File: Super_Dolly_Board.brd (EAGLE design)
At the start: 154.5 x 44.5 mm, 89 parts, among them IC1 AT90USB646-AU, J1 10118193-0001LF, J3 SJ1-2503A, J4 RJHS-538X, J5 SJ1-2503A, P1 TC33X-2, SW1 SKQUDBE010, U1 AT90USB646-MU, U2 MMDT3904, U3 TB6559FG, U4 TS2937CW50, U5 TB6559FG, U6 SN75176BDR, U7 TB6559FG, U8 TPD2E007DCK, U9 TS2937CW50, X1 3.2X2.5MMCRYSTAL

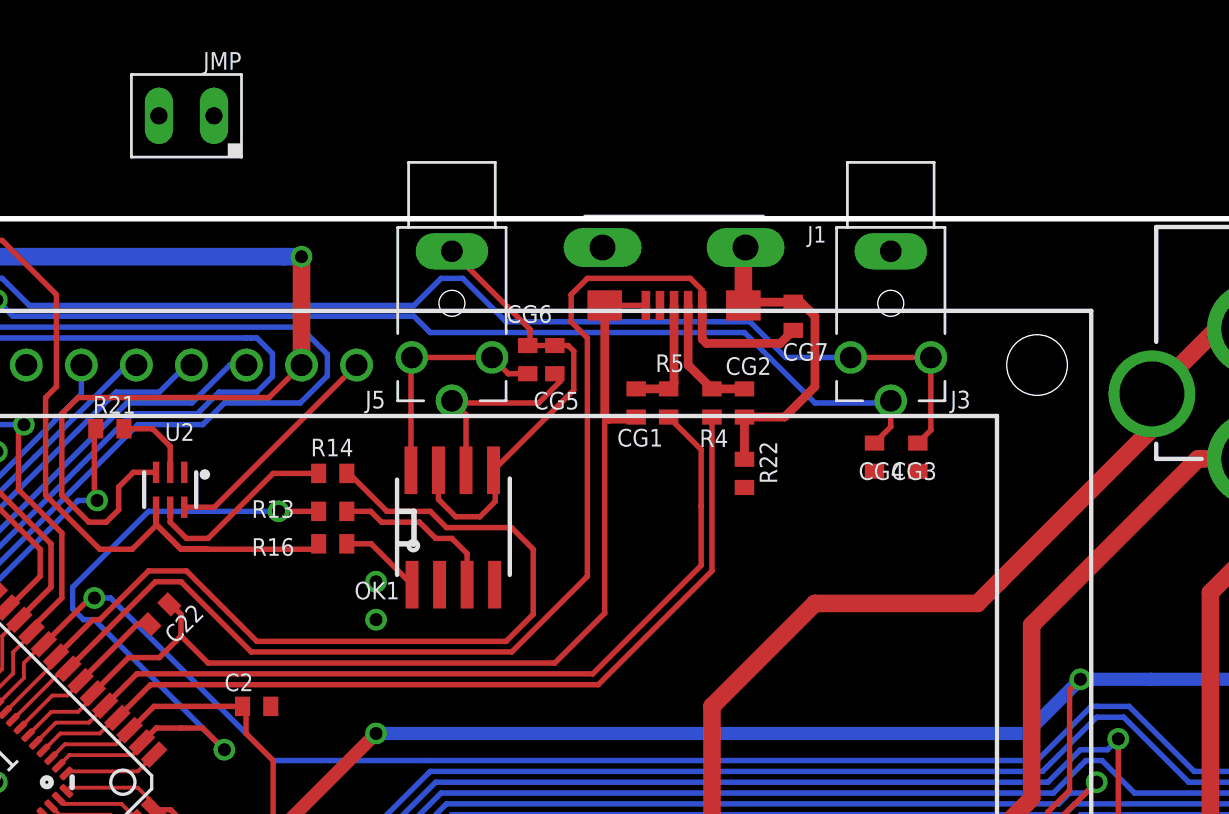
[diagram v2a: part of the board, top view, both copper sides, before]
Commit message: added jumper to bridge VUSB and +5V so the usb can power the device for testing
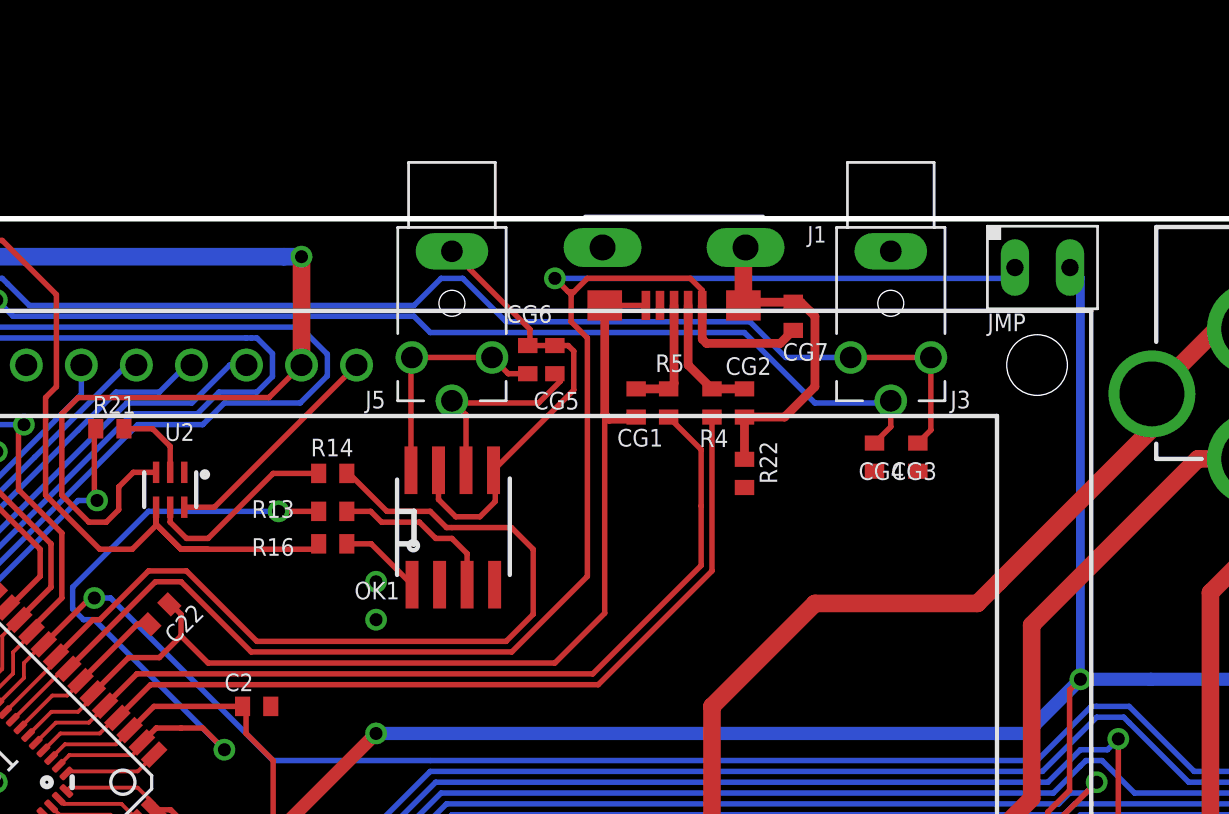
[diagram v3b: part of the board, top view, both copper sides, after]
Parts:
- moved JMP 40.1 mm to (37.8, 16.8), turned to 0 degrees
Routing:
- net VUSB: track 60.2 -> 82.7 mm, vias 0 -> 1
- net +5V: track 473.1 -> 492.3 mm
- net GND: vias 47 -> 111
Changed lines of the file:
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@@
 <element name="R26" library="parkers_parts" package="0402_RES" value="20K" x="7.5" y="-16.25" rot="R180"/>
 <element name="U1" library="at90usb" package="MLF64" value="AT90USB646-MU" x="-13" y="-7" rot="R225"/>
-<element name="JMP" library="parkers_parts" package="P1X02" value="P1X02PH" x="-1.75" y="23.75" rot="R180"/>
+<element name="JMP" library="parkers_parts" package="P1X02" value="P1X02PH" x="37.75" y="16.75"/>
 </elements>
 <signals>
@@
 <via x="77.75" y="-7.5" extent="1-16" drill="0.6"/>
 <wire x1="77.75" y1="-7.5" x2="77.25" y2="-7.5" width="0.254" layer="16"/>
+<wire x1="39.02" y1="16.75" x2="39.5" y2="16.27" width="0.4064" layer="16"/>
+<wire x1="39.5" y1="16.27" x2="39.5" y2="-2.25" width="0.4064" layer="16"/>
 <wire x1="-6" y1="-17.5" x2="-7.45961875" y2="-17.631546875" width="0" layer="19" extent="1-16"/>
-<wire x1="-3.02" y1="23.75" x2="2.75" y2="17.25" width="0" layer="19" extent="16-16"/>
 </signal>
 <signal name="GND">
@@
 <via x="50.25" y="-21.75" extent="1-16" drill="0.6"/>
 <via x="48.75" y="-21.75" extent="1-16" drill="0.6"/>
+<via x="24.5" y="-11" extent="1-16" drill="0.6"/>
+<via x="28.5" y="-11" extent="1-16" drill="0.6"/>
+<via x="27.25" y="-11" extent="1-16" drill="0.6"/>
+<via x="25.75" y="-11" extent="1-16" drill="0.6"/>
+<via x="24.5" y="-12.5" extent="1-16" drill="0.6"/>
+<via x="28.5" y="-12.5" extent="1-16" drill="0.6"/>
+<via x="27.25" y="-12.5" extent="1-16" drill="0.6"/>
+<via x="25.75" y="-12.5" extent="1-16" drill="0.6"/>
+<via x="24.5" y="-14" extent="1-16" drill="0.6"/>
+<via x="28.5" y="-14" extent="1-16" drill="0.6"/>
+<via x="27.25" y="-14" extent="1-16" drill="0.6"/>
+<via x="25.75" y="-14" extent="1-16" drill="0.6"/>
+<via x="24.5" y="-15.5" extent="1-16" drill="0.6"/>
+<via x="28.5" y="-15.5" extent="1-16" drill="0.6"/>
+<via x="27.25" y="-15.5" extent="1-16" drill="0.6"/>
+<via x="25.75" y="-15.5" extent="1-16" drill="0.6"/>
+<via x="24.5" y="-17.25" extent="1-16" drill="0.6"/>
+<via x="28.5" y="-17.25" extent="1-16" drill="0.6"/>
+<via x="27.25" y="-17.25" extent="1-16" drill="0.6"/>
+<via x="25.75" y="-17.25" extent="1-16" drill="0.6"/>
+<via x="24.5" y="-18.75" extent="1-16" drill="0.6"/>
+<via x="28.5" y="-18.75" extent="1-16" drill="0.6"/>
+<via x="27.25" y="-18.75" extent="1-16" drill="0.6"/>
+<via x="25.75" y="-18.75" extent="1-16" drill="0.6"/>
+<via x="24.5" y="-20.25" extent="1-16" drill="0.6"/>
+<via x="28.5" y="-20.25" extent="1-16" drill="0.6"/>
+<via x="27.25" y="-20.25" extent="1-16" drill="0.6"/>
+<via x="25.75" y="-20.25" extent="1-16" drill="0.6"/>
+<via x="24.5" y="-21.75" extent="1-16" drill="0.6"/>
+<via x="28.5" y="-21.75" extent="1-16" drill="0.6"/>
+<via x="27.25" y="-21.75" extent="1-16" drill="0.6"/>
+<via x="25.75" y="-21.75" extent="1-16" drill="0.6"/>
+<via x="67" y="-11.5" extent="1-16" drill="0.6"/>
+<via x="71" y="-11.5" extent="1-16" drill="0.6"/>
+<via x="69.75" y="-11.5" extent="1-16" drill="0.6"/>
+<via x="68.25" y="-11.5" extent="1-16" drill="0.6"/>
+<via x="67" y="-13" extent="1-16" drill="0.6"/>
+<via x="71" y="-13" extent="1-16" drill="0.6"/>
+<via x="69.75" y="-13" extent="1-16" drill="0.6"/>
+<via x="68.25" y="-13" extent="1-16" drill="0.6"/>
+<via x="67" y="-14.5" extent="1-16" drill="0.6"/>
+<via x="71" y="-14.5" extent="1-16" drill="0.6"/>
+<via x="69.75" y="-14.5" extent="1-16" drill="0.6"/>
+<via x="68.25" y="-14.5" extent="1-16" drill="0.6"/>
+<via x="67" y="-16" extent="1-16" drill="0.6"/>
+<via x="71" y="-16" extent="1-16" drill="0.6"/>
+<via x="69.75" y="-16" extent="1-16" drill="0.6"/>
+<via x="68.25" y="-16" extent="1-16" drill="0.6"/>
+<via x="67" y="-17.25" extent="1-16" drill="0.6"/>
+<via x="71" y="-17.25" extent="1-16" drill="0.6"/>
+<via x="69.75" y="-17.25" extent="1-16" drill="0.6"/>
+<via x="68.25" y="-17.25" extent="1-16" drill="0.6"/>
+<via x="67" y="-18.75" extent="1-16" drill="0.6"/>
+<via x="71" y="-18.75" extent="1-16" drill="0.6"/>
+<via x="69.75" y="-18.75" extent="1-16" drill="0.6"/>
+<via x="68.25" y="-18.75" extent="1-16" drill="0.6"/>
+<via x="67" y="-20.25" extent="1-16" drill="0.6"/>
+<via x="71" y="-20.25" extent="1-16" drill="0.6"/>
+<via x="69.75" y="-20.25" extent="1-16" drill="0.6"/>
+<via x="68.25" y="-20.25" extent="1-16" drill="0.6"/>
+<via x="67" y="-21.75" extent="1-16" drill="0.6"/>
+<via x="71" y="-21.75" extent="1-16" drill="0.6"/>
+<via x="69.75" y="-21.75" extent="1-16" drill="0.6"/>
+<via x="68.25" y="-21.75" extent="1-16" drill="0.6"/>
 </signal>
 <signal name="AREF" class="4">
@@
 <wire x1="22.05" y1="15.7" x2="21.5" y2="16.25" width="0.254" layer="1"/>
 <wire x1="21.5" y1="16.25" x2="16.75" y2="16.25" width="0.254" layer="1"/>
-<wire x1="16.75" y1="16.25" x2="16" y2="15.5" width="0.254" layer="1"/>
+<wire x1="16.75" y1="16.25" x2="16.125" y2="15.625" width="0.254" layer="1"/>
+<wire x1="16.125" y1="15.625" x2="16" y2="15.5" width="0.254" layer="1"/>
 <wire x1="16" y1="15.5" x2="16" y2="14.25" width="0.254" layer="1"/>
 <wire x1="16" y1="14.25" x2="16.75" y2="13.5" width="0.254" layer="1"/>
@@
 <wire x1="-2" y1="2.25" x2="-3.1843125" y2="2.25" width="0.254" layer="1"/>
 <wire x1="-3.1843125" y1="2.25" x2="-7.201721875" y2="-1.767409375" width="0.254" layer="1"/>
-<wire x1="16" y1="15.5" x2="-0.48" y2="23.75" width="0" layer="19" extent="1-1"/>
+<wire x1="36.48" y1="16.75" x2="35.98" y2="16.25" width="0.254" layer="16"/>
+<wire x1="35.98" y1="16.25" x2="15.25" y2="16.25" width="0.254" layer="16"/>
+<via x="15.25" y="16.25" extent="1-16" drill="0.6"/>
+<wire x1="15.25" y1="16.25" x2="15.875" y2="15.625" width="0.254" layer="1"/>
+<wire x1="15.875" y1="15.625" x2="16.125" y2="15.625" width="0.254" layer="1"/>
 </signal>
 <signal name="UCAP">
@@
 <wire x1="-18.596190625" y1="-6" x2="-18.35633125" y2="-6.239859375" width="0" layer="19" extent="1-1"/>
 </signal>
-<signal name="GND1">
-<via x="67" y="-11.5" extent="1-16" drill="0.6"/>
-<via x="71" y="-11.5" extent="1-16" drill="0.6"/>
-<via x="69.75" y="-11.5" extent="1-16" drill="0.6"/>
-<via x="68.25" y="-11.5" extent="1-16" drill="0.6"/>
-<via x="67" y="-13" extent="1-16" drill="0.6"/>
-<via x="71" y="-13" extent="1-16" drill="0.6"/>
-<via x="69.75" y="-13" extent="1-16" drill="0.6"/>
-<via x="68.25" y="-13" extent="1-16" drill="0.6"/>
-<via x="67" y="-14.5" extent="1-16" drill="0.6"/>
-<via x="71" y="-14.5" extent="1-16" drill="0.6"/>
-<via x="69.75" y="-14.5" extent="1-16" drill="0.6"/>
-<via x="68.25" y="-14.5" extent="1-16" drill="0.6"/>
-<via x="67" y="-16" extent="1-16" drill="0.6"/>
-<via x="71" y="-16" extent="1-16" drill="0.6"/>
-<via x="69.75" y="-16" extent="1-16" drill="0.6"/>
-<via x="68.25" y="-16" extent="1-16" drill="0.6"/>
-</signal>
-<signal name="GND2">
-<via x="67" y="-17.25" extent="1-16" drill="0.6"/>
-<via x="71" y="-17.25" extent="1-16" drill="0.6"/>
-<via x="69.75" y="-17.25" extent="1-16" drill="0.6"/>
-<via x="68.25" y="-17.25" extent="1-16" drill="0.6"/>
-<via x="67" y="-18.75" extent="1-16" drill="0.6"/>
-<via x="71" y="-18.75" extent="1-16" drill="0.6"/>
-<via x="69.75" y="-18.75" extent="1-16" drill="0.6"/>
-<via x="68.25" y="-18.75" extent="1-16" drill="0.6"/>
-<via x="67" y="-20.25" extent="1-16" drill="0.6"/>
-<via x="71" y="-20.25" extent="1-16" drill="0.6"/>
-<via x="69.75" y="-20.25" extent="1-16" drill="0.6"/>
-<via x="68.25" y="-20.25" extent="1-16" drill="0.6"/>
-<via x="67" y="-21.75" extent="1-16" drill="0.6"/>
-<via x="71" y="-21.75" extent="1-16" drill="0.6"/>
-<via x="69.75" y="-21.75" extent="1-16" drill="0.6"/>
-<via x="68.25" y="-21.75" extent="1-16" drill="0.6"/>
-</signal>
-<signal name="GND3">
-<via x="24.5" y="-11" extent="1-16" drill="0.6"/>
-<via x="28.5" y="-11" extent="1-16" drill="0.6"/>
-<via x="27.25" y="-11" extent="1-16" drill="0.6"/>
-<via x="25.75" y="-11" extent="1-16" drill="0.6"/>
-<via x="24.5" y="-12.5" extent="1-16" drill="0.6"/>
-<via x="28.5" y="-12.5" extent="1-16" drill="0.6"/>
-<via x="27.25" y="-12.5" extent="1-16" drill="0.6"/>
-<via x="25.75" y="-12.5" extent="1-16" drill="0.6"/>
-<via x="24.5" y="-14" extent="1-16" drill="0.6"/>
-<via x="28.5" y="-14" extent="1-16" drill="0.6"/>
-<via x="27.25" y="-14" extent="1-16" drill="0.6"/>
-<via x="25.75" y="-14" extent="1-16" drill="0.6"/>
-<via x="24.5" y="-15.5" extent="1-16" drill="0.6"/>
-<via x="28.5" y="-15.5" extent="1-16" drill="0.6"/>
-<via x="27.25" y="-15.5" extent="1-16" drill="0.6"/>
-<via x="25.75" y="-15.5" extent="1-16" drill="0.6"/>
-</signal>
-<signal name="GND4">
-<via x="24.5" y="-17.25" extent="1-16" drill="0.6"/>
-<via x="28.5" y="-17.25" extent="1-16" drill="0.6"/>
-<via x="27.25" y="-17.25" extent="1-16" drill="0.6"/>
-<via x="25.75" y="-17.25" extent="1-16" drill="0.6"/>
-<via x="24.5" y="-18.75" extent="1-16" drill="0.6"/>
-<via x="28.5" y="-18.75" extent="1-16" drill="0.6"/>
-<via x="27.25" y="-18.75" extent="1-16" drill="0.6"/>
-<via x="25.75" y="-18.75" extent="1-16" drill="0.6"/>
-<via x="24.5" y="-20.25" extent="1-16" drill="0.6"/>
-<via x="28.5" y="-20.25" extent="1-16" drill="0.6"/>
-<via x="27.25" y="-20.25" extent="1-16" drill="0.6"/>
-<via x="25.75" y="-20.25" extent="1-16" drill="0.6"/>
-<via x="24.5" y="-21.75" extent="1-16" drill="0.6"/>
-<via x="28.5" y="-21.75" extent="1-16" drill="0.6"/>
-<via x="27.25" y="-21.75" extent="1-16" drill="0.6"/>
-<via x="25.75" y="-21.75" extent="1-16" drill="0.6"/>
-</signal>
 </signals>
-<errors>
-</errors>
 </board>
 </drawing>

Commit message: finished SDB REV2
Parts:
- removed R25: 36K, parkers_parts:0402_RES
- removed R26: 20K, parkers_parts:0402_RES
- added C14: .1uF, parkers_parts:0402_CAP
- added D2: PMEG6010EP, parkers_parts:SOD-128
- added U10: IP4234CZ6, parkers_parts:SOT-457
- C10, C11, C8: value .1uF -> .1uF 35V
- D1: value PMEG3030EP -> PMEG6010EP
- J4: value RJHS-538X -> RJHSE-5381
- MOT0, MOT1, MOT2: value (none) -> KLDX-0202-B-LT
- PWR: value (none) -> KLDX-0202-A-LT
- R4: value 22 -> 4K
- R5: value 22 -> 20K
- moved CG4 69.0 mm to (-34.8, -9.50), turned to 270 degrees
- moved CG7 64.0 mm to (-37.0, 4.50), turned to 180 degrees
- moved CG1 60.1 mm to (-40.8, 4.50), turned to 180 degrees
- moved R5 31.6 mm to (7.50, -18.2), turned to 0 degrees
- moved R4 30.7 mm to (7.50, -16.2), turned to 180 degrees
- moved CG2 6.50 mm to (30.0, 8.00)
- moved R22 4.37 mm to (25.0, 11.5)
- moved CG3 2.00 mm to (32.0, 8.00)
- renumbered IC1 to U11
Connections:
- net 12VB: now also D2.CATHODE
- net BATT_V: now also C14.1, R4.2, R5.1; no longer R25.1, R26.2
- net COM1: now also CG4.1
- net COM2: now also CG7.1
- net COM3: now also CG1.2
- net D+: now also U10.1; no longer CG1.2, R5.1
- net D-: now also U10.6; no longer CG2.2, R4.1
- net GND: now also C14.2, CG1.1, CG2.1, CG4.2, CG7.2, D2.ANODE, R4.1; no longer CG4.1, R26.1
- net IO_2: now also CG2.2; no longer CG3.2
- net IO_3: now also CG3.2; no longer CG4.2
- net RD+: now also U10.3; no longer R5.2
- net RD-: now also U10.4; no longer R4.2
- net UGND: now also U10.2; no longer CG1.1, CG2.1, CG7.1
- net VIN: now also R5.2; no longer R25.2
- net VUSB: now also U10.5; no longer CG7.2
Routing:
- net GND: track 17.6 -> 48.6 mm, vias 111 -> 177
- net M2_P: track 114.2 -> 103.2 mm
- net UGND: track 67.8 -> 59.4 mm
- net COM2: track 46.2 -> 52.8 mm, vias 0 -> 2
- net 12VB: track 29.9 -> 33.0 mm
- net OK_SHT: track 55.4 -> 53.2 mm
- net COM3: track 45.7 -> 47.5 mm
- net BATT_V: track 20.7 -> 22.4 mm
- net RD-: track 41.4 -> 39.7 mm
- net M1_A: track 110.3 -> 111.9 mm
- net RD+: track 41.6 -> 40.1 mm
- net COM1: track 51.5 -> 52.8 mm
- net M2_B: track 101.2 -> 102.0 mm
- net M1_B: track 94.3 -> 95.0 mm
- net +5V: track 492.3 -> 493.0 mm
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
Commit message: finished REV2 of SDB
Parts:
- added AUX: (no value), pinhead:2X04
- added CG8, CG9: CG0402MLC-05LG, parkers_parts:0402_RES
- added J6: SJ1-2503A, parkers_parts:SJ1-2503A
- LCD1: value LCD-16X2 -> LCD-16X2NOHOLES; device SparkFun:LCD-16X2 -> SparkFun-Displays:LCD-16X2_NOHOLES
- moved CG6 53.3 mm to (-39.0, 7.25), turned to 90 degrees
- moved CG5 47.1 mm to (-31.5, 6.75)
- moved J5 47.0 mm to (-36.5, 17.5)
- moved OK1 45.5 mm to (-33.0, 2.37)
- moved R13 18.4 mm to (-13.2, 8.00), turned to 90 degrees
- moved CG7 16.5 mm to (-37.5, -12.0), turned to 0 degrees
- moved LOGO3 12.0 mm to (1.75, -25.0)
- moved U$2 10.2 mm to (-27.5, 16.8)
- moved R15 8.25 mm to (-40.8, 16.0)
- moved R14 7.85 mm to (-2.25, 4.25), turned to 45 degrees
- moved R16 7.11 mm to (-0.50, 8.50), turned to 180 degrees
- moved R5 6.01 mm to (7.25, -12.2)
- moved U2 6.01 mm to (3.50, 6.25), turned to 90 degrees
- moved R4 5.26 mm to (7.25, -11.0)
- moved C14 4.76 mm to (7.25, -9.75)
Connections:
- removed net PE4: U1.18, U11.18
- removed net PE5: U1.19, U11.19
- removed net PE6: U1.1, U11.1
- new net PB5: U1.15, U11.15
- new net PB6: U1.16, U11.16
- new net PD7: U1.32, U11.32
- net +5V: now also AUX.1
- net COM1: now also U1.14, U11.14; no longer U1.32, U11.32
- net FOC: now also U1.17, U11.17; no longer U1.2, U11.2
- net GND: now also AUX.2, CG8.1, CG9.1, J6.1
- net IO_0: now also CG8.2, J6.2, J6.3, U1.18, U11.18; no longer U1.14, U11.14
- net IO_1: now also CG9.2, J6.4, U1.19, U11.19; no longer U1.15, U11.15
- net IO_2: now also U1.1, U11.1; no longer U1.16, U11.16
- net IO_3: now also U1.2, U11.2; no longer U1.17, U11.17
- net PF2: now also AUX.3
- net PF3: now also AUX.4
- net PF4: now also AUX.5
- net PF5: now also AUX.6
- net PF6: now also AUX.7
- net PF7: now also AUX.8
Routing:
- net N$23: track 3.79 -> 54.9 mm, vias 0 -> 2
- net IO_1: track 4.28 -> 53.2 mm
- net IO_0: track 4.17 -> 51.6 mm
- net SHT: track 41.9 -> 10.8 mm
- net COM1: track 52.8 -> 83.1 mm, vias 0 -> 2
- net PF7: track 3.80 -> 30.5 mm
- net PF5: track 3.54 -> 28.4 mm
- net PF3: track 3.69 -> 28.2 mm
- net FOC: track 32.4 -> 9.43 mm, vias 2 -> 0
- net PF6: track 3.66 -> 26.4 mm
- net N$5: track 3.67 -> 25.4 mm
- net PF4: track 3.54 -> 25.2 mm
- net PF2: track 3.89 -> 25.1 mm
- net N$22: track 7.79 -> 28.3 mm, vias 0 -> 2
- net IO_2: track 63.8 -> 78.5 mm
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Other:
- board text added: "Super Dolly Board REV 2"
- board text removed: "Super Dolly Board REV 1"
